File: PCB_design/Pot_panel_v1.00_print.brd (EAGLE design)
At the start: 39 x 25.4 mm, 5 parts

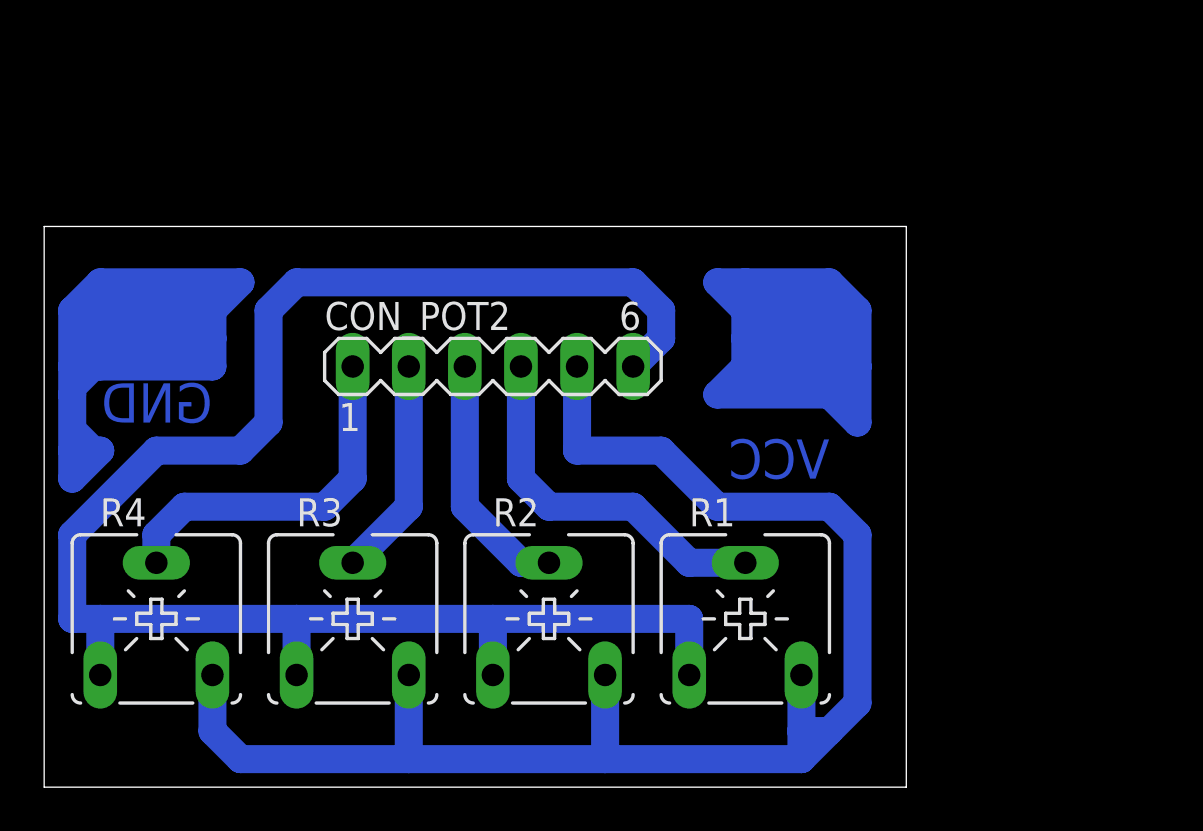
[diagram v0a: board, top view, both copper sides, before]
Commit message: Change arduino layout to fit to the buyable clone
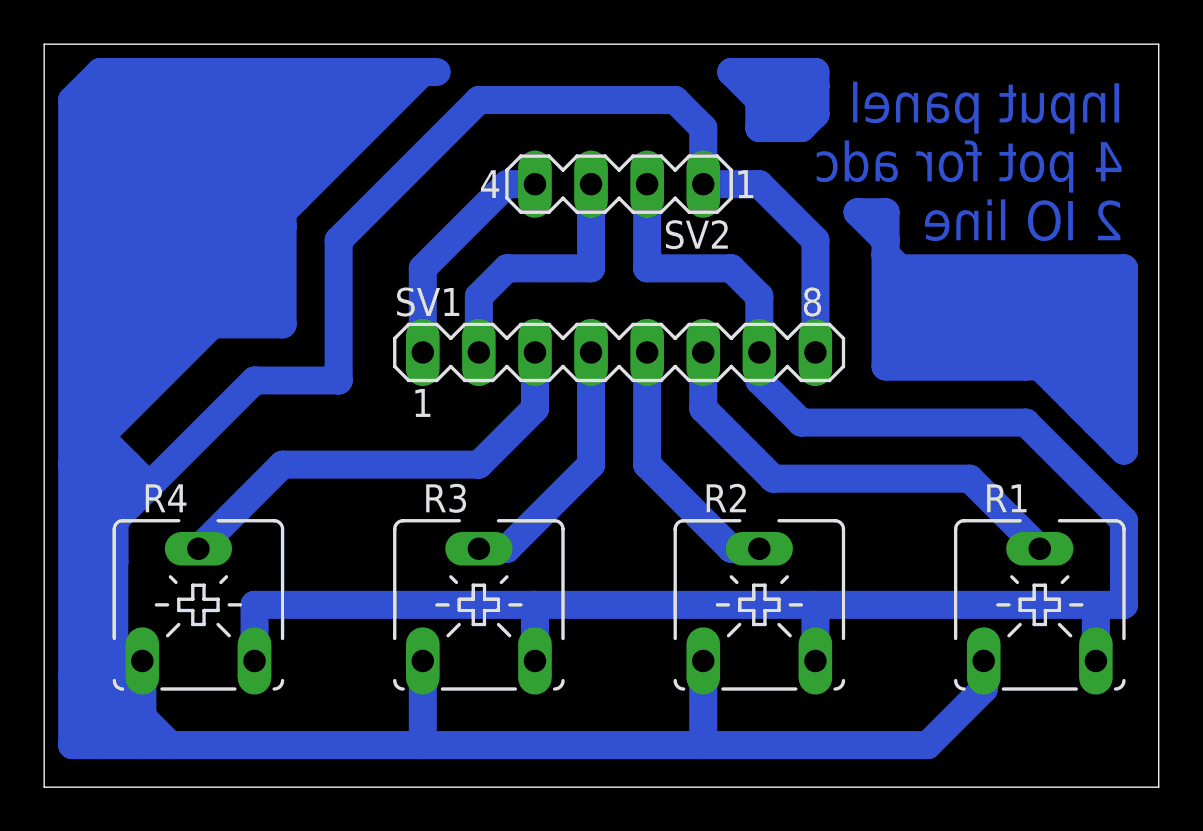
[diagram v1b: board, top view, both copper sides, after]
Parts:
- removed CON_POT2: (no value), con-lstb:MA06-1
- added SV1: (no value), con-lstb:MA08-1
- added SV2: (no value), con-lstb:MA04-1
- moved R1 13.4 mm to (45.1, 8.26)
- moved R2 9.55 mm to (32.4, 8.26)
- moved R3 5.75 mm to (19.7, 8.26)
- moved R4 2.01 mm to (6.99, 8.26)
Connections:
- new net IO1: SV1.1, SV2.4
- new net IO2: SV1.2, SV2.3
- net A0: now also SV1.6; no longer CON_POT2.4
- net A1: now also SV1.5; no longer CON_POT2.3
- net A2: now also SV1.4; no longer CON_POT2.2
- net A3: now also SV1.3; no longer CON_POT2.1
- net GND: now also SV1.8, SV2.1; no longer CON_POT2.6
- net VCC: now also SV1.7, SV2.2; no longer CON_POT2.5
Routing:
- net GND: track 79.9 -> 398.2 mm
- net N$3: track 0.00 -> 52.9 mm
- net N$2: track 51.2 -> 0.00 mm
- net N$1: track 48.1 -> 0.00 mm
- net N$4: track 0.00 -> 18.5 mm
- net VCC: track 71.7 -> 85.7 mm
- net IO2: track 0.00 -> 12.0 mm
- net IO1: track 0.00 -> 10.5 mm
- net A3: track 16.3 -> 20.4 mm
- net A0: track 16.8 -> 20.4 mm
- net A2: track 9.94 -> 11.7 mm
- net A1: track 11.2 -> 11.7 mm
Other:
- board size 39 x 25.4 mm -> 50.5 x 33.6 mm
- board text added: "Input panel 4 pot for adc 2 IO line"
- board text removed: "GND"
- board text removed: "VCC"
